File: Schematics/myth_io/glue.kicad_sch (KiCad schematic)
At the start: 4 parts, among them U1 74HC14, U2 74LS02, U5 74AHC04, U6 74HC74

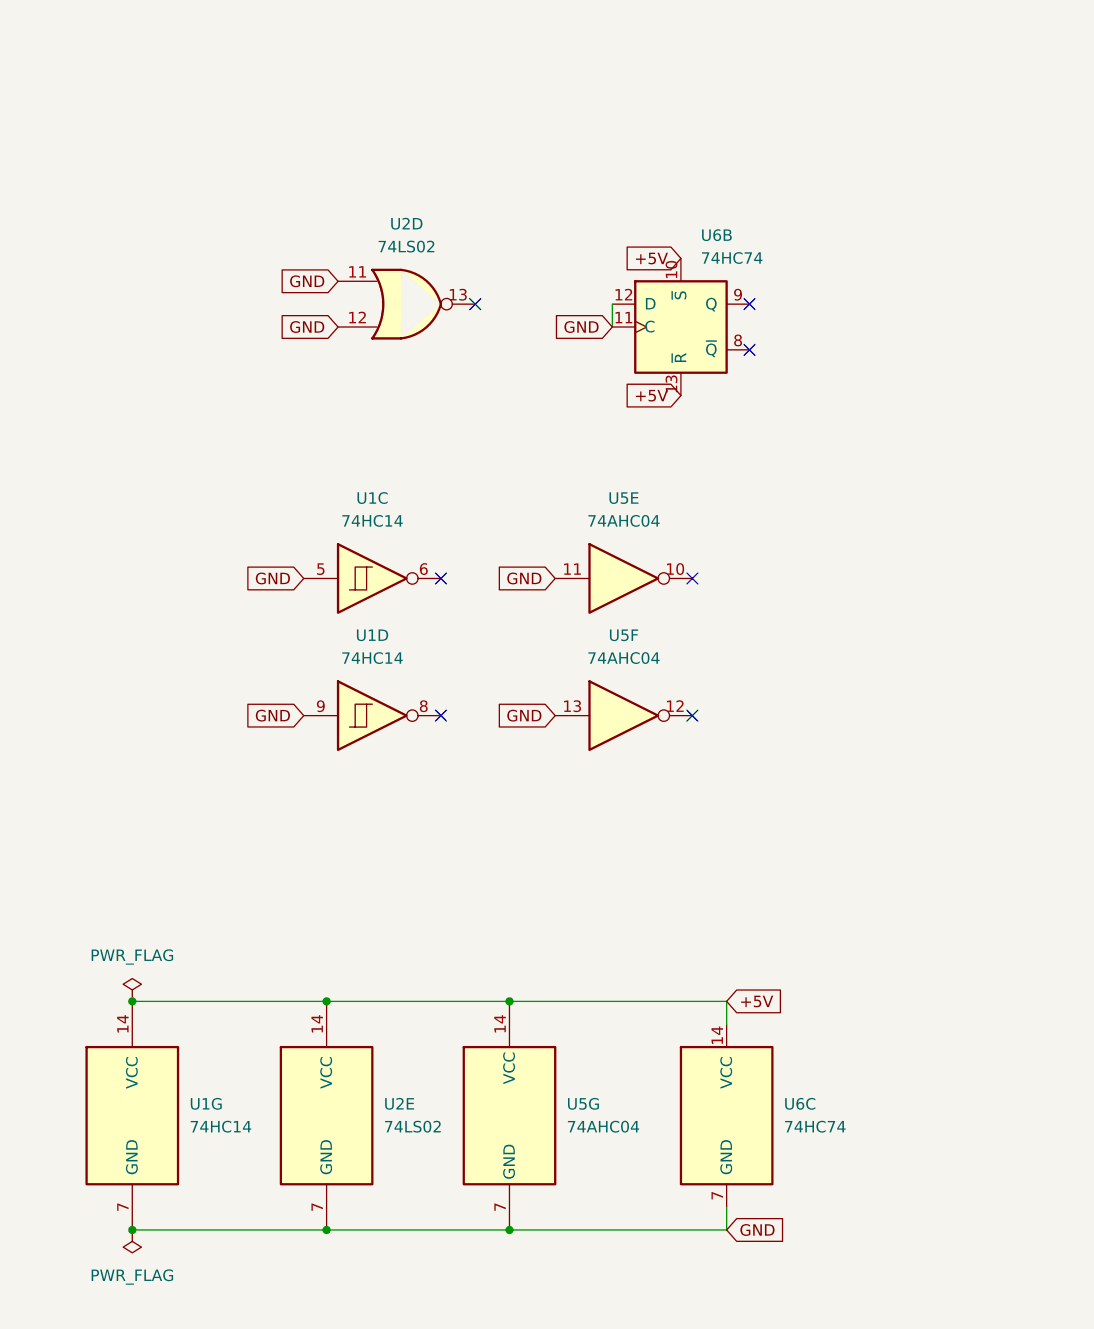
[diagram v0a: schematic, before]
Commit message: Change d to g
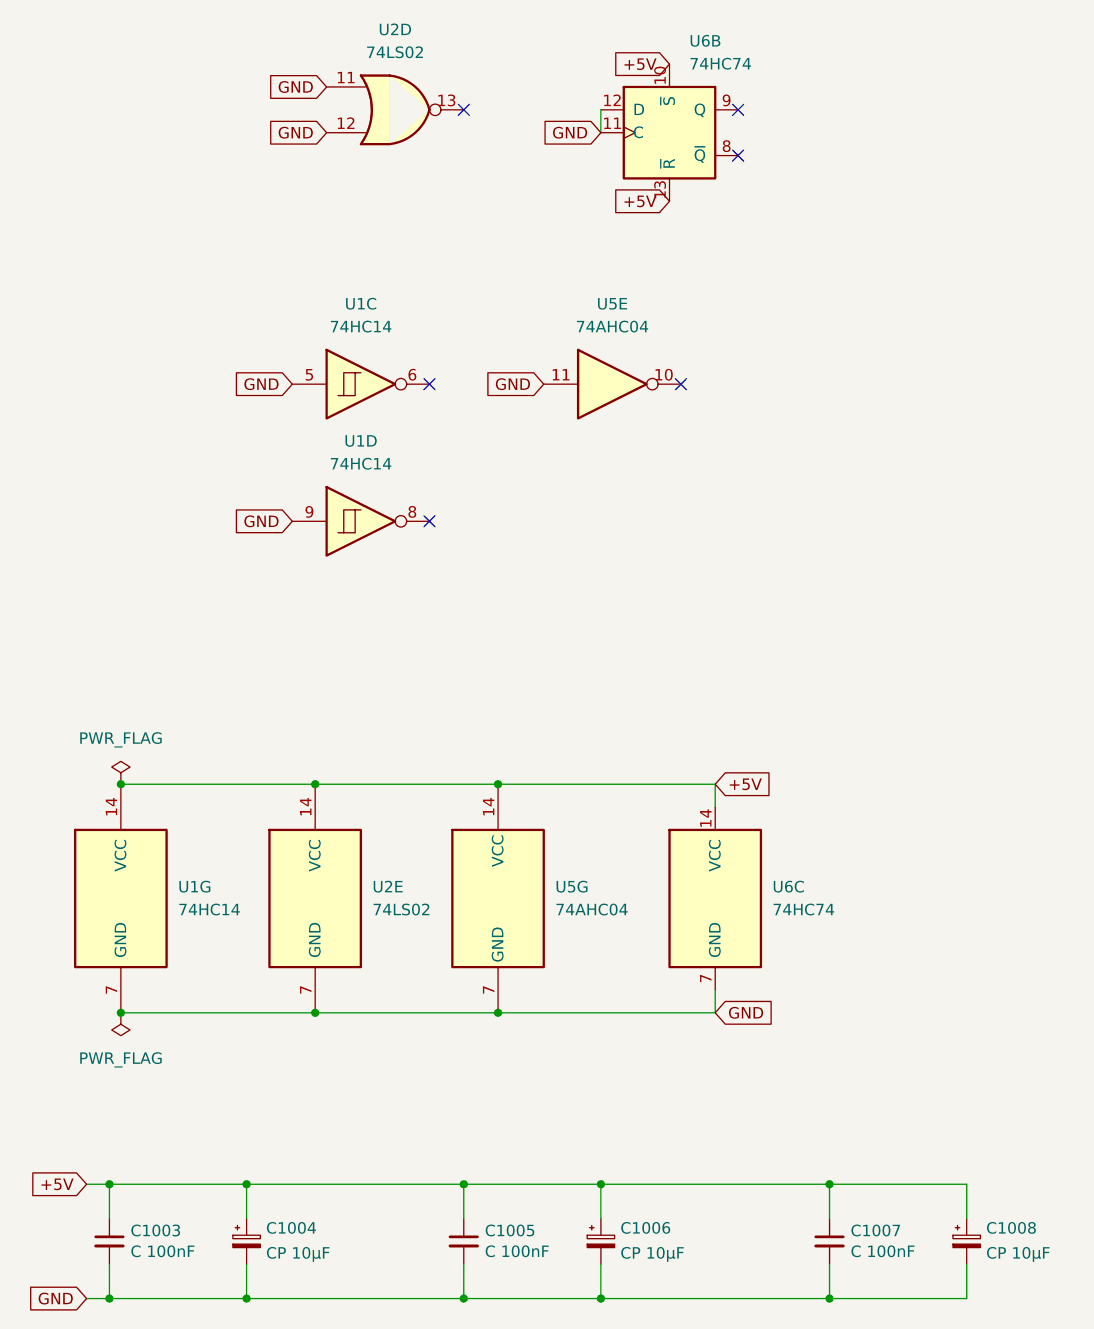
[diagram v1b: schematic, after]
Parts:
- removed unit 6 of U5
- added C1003, C1005, C1007: C 100nF, Capacitor_THT:C_Disc_D5.0mm_W2.5mm_P2.50mm, symbol Device:C_Small
- added C1004, C1006, C1008: CP 10μF, Capacitor_THT:CP_Radial_D6.3mm_P2.50mm, symbol Device:C_Polarized_Small
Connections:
- net +5V: now also C1003.1, C1004.1, C1005.1, C1006.1, C1007.1, C1008.1
- net GND: now also C1003.2, C1004.2, C1005.2, C1006.2, C1007.2, C1008.2
- no-connect marks 7 -> 6
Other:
- moved on the sheet: U1C, U1D, U1G, U2D, U2E, U5E, U5G, U6B, U6C

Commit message: Change CO do D
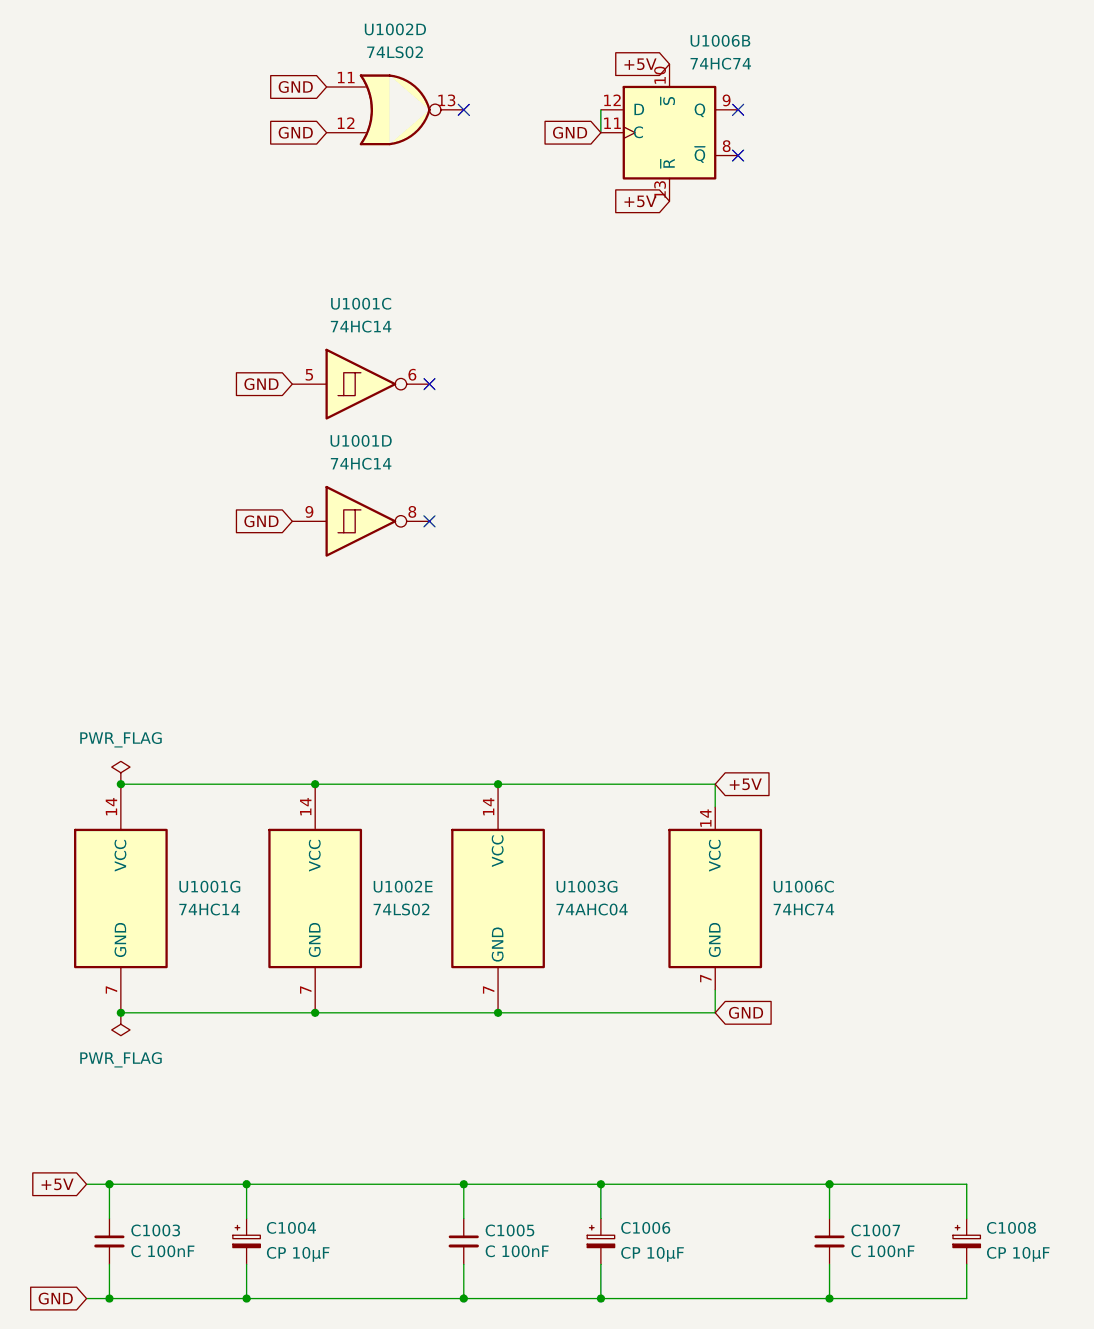
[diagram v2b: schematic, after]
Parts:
- removed unit 5 of U5
- renumbered U1 to U1001, U2 to U1002, U5 to U1003, U6 to U1006
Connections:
- no-connect marks 6 -> 5
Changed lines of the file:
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@@
-	)
-	(no_connect
-		(at 111.76 74.93)
 	)
 	(no_connect
@@
 	(global_label "GND"
 		(shape input)
-		(at 96.52 74.93 180)
+		(at 115.57 144.78 0)
 		(fields_autoplaced yes)
 		(effects
@@
 				(size 1.27 1.27)
 			)
-			(justify right)
+			(justify left)
 		)
 		(property "Intersheetrefs" "${INTERSHEET_REFS}"
-			(at 89.6643 74.93 0)
-			(effects
-				(font
-					(size 1.27 1.27)
-				)
-				(justify right)
+			(at 122.4257 144.78 0)
+			(effects
+				(font
+					(size 1.27 1.27)
+				)
+				(justify left)
 				(hide yes)
 			)
@@
 	(global_label "GND"
 		(shape input)
-		(at 115.57 144.78 0)
+		(at 68.58 90.17 180)
 		(fields_autoplaced yes)
 		(effects
@@
 				(size 1.27 1.27)
 			)
-			(justify left)
-		)
-		(property "Intersheetrefs" "${INTERSHEET_REFS}"
-			(at 122.4257 144.78 0)
-			(effects
-				(font
-					(size 1.27 1.27)
-				)
-				(justify left)
-				(hide yes)
-			)
-		)
-	)
-	(global_label "GND"
-		(shape input)
-		(at 68.58 90.17 180)
-		(fields_autoplaced yes)
-		(effects
-			(font
-				(size 1.27 1.27)
-			)
 			(justify right)
 		)
@@
 				(justify right)
 				(hide yes)
-			)
-		)
-	)
-	(symbol
-		(lib_id "74xx:74AHC04")
-		(at 104.14 74.93 0)
-		(unit 5)
-		(exclude_from_sim no)
-		(in_bom yes)
-		(on_board yes)
-		(dnp no)
-		(fields_autoplaced yes)
-		(property "Reference" "U5"
-			(at 104.14 66.04 0)
-			(effects
-				(font
-					(size 1.27 1.27)
-				)
-			)
-		)
-		(property "Value" "74AHC04"
-			(at 104.14 68.58 0)
-			(effects
-				(font
-					(size 1.27 1.27)
-				)
-			)
-		)
-		(property "Footprint" "Package_DIP:DIP-14_W7.62mm_Socket_LongPads"
-			(at 104.14 74.93 0)
-			(effects
-				(font
-					(size 1.27 1.27)
-				)
-				(hide yes)
-			)
-		)
-		(property "Datasheet" "https://assets.nexperia.com/documents/data-sheet/74AHC_AHCT04.pdf"
-			(at 104.14 74.93 0)
-			(effects
-				(font
-					(size 1.27 1.27)
-				)
-				(hide yes)
-			)
-		)
-		(property "Description" "Hex Inverter"
-			(at 104.14 74.93 0)
-			(effects
-				(font
-					(size 1.27 1.27)
-				)
-				(hide yes)
-			)
-		)
-		(pin "6"
-		)
-		(pin "13"
-		)
-		(pin "14"
-		)
-		(pin "7"
-		)
-		(pin "12"
-		)
-		(pin "1"
-		)
-		(pin "10"
-		)
-		(pin "11"
-		)
-		(pin "5"
-		)
-		(pin "4"
-		)
-		(pin "8"
-		)
-		(pin "2"
-		)
-		(pin "3"
-		)
-		(pin "9"
-		)
-		(instances
-			(project "myth_io"
-				(path "/a907dd88-e0e4-4e6e-a291-053f6213a316/23f7cdcd-5710-47e5-9933-2b44d7b8056b"
-					(reference "U5")
-					(unit 5)
-				)
 			)
 		)
@@
 		(dnp no)
 		(fields_autoplaced yes)
-		(property "Reference" "U2"
+		(property "Reference" "U1002"
 			(at 77.47 130.8099 0)
 			(effects
@@
 			(project "myth_io"
 				(path "/a907dd88-e0e4-4e6e-a291-053f6213a316/23f7cdcd-5710-47e5-9933-2b44d7b8056b"
-					(reference "U2")
+					(reference "U1002")
 					(unit 5)
 				)
@@
 		(dnp no)
 		(fields_autoplaced yes)
-		(property "Reference" "U6"
+		(property "Reference" "U1006"
 			(at 121.92 130.8099 0)
 			(effects
@@
 			(project "myth_io"
 				(path "/a907dd88-e0e4-4e6e-a291-053f6213a316/23f7cdcd-5710-47e5-9933-2b44d7b8056b"
-					(reference "U6")
+					(reference "U1006")
 					(unit 3)
 				)
@@
 		(on_board yes)
 		(dnp no)
-		(property "Reference" "#FLG02"
+		(property "Reference" "#FLG01002"
 			(at 49.53 146.685 0)
 			(effects
@@
 			(project "myth_io"
 				(path "/a907dd88-e0e4-4e6e-a291-053f6213a316/23f7cdcd-5710-47e5-9933-2b44d7b8056b"
-					(reference "#FLG02")
+					(reference "#FLG01002")
 					(unit 1)
 				)
@@
 		(dnp no)
 		(fields_autoplaced yes)
-		(property "Reference" "#FLG01"
+		(property "Reference" "#FLG01001"
 			(at 49.53 117.475 0)
 			(effects
@@
 			(project "myth_io"
 				(path "/a907dd88-e0e4-4e6e-a291-053f6213a316/23f7cdcd-5710-47e5-9933-2b44d7b8056b"
-					(reference "#FLG01")
+					(reference "#FLG01001")
 					(unit 1)
 				)
@@
 		(dnp no)
 		(fields_autoplaced yes)
-		(property "Reference" "U6"
+		(property "Reference" "U1006"
 			(at 112.6841 36.83 0)
 			(effects
@@
 			(project "myth_io"
 				(path "/a907dd88-e0e4-4e6e-a291-053f6213a316/23f7cdcd-5710-47e5-9933-2b44d7b8056b"
-					(reference "U6")
+					(reference "U1006")
 					(unit 2)
 				)
@@
 		(dnp no)
 		(fields_autoplaced yes)
-		(property "Reference" "U5"
+		(property "Reference" "U1003"
 			(at 97.79 130.8099 0)
 			(effects
@@
 			(project "myth_io"
 				(path "/a907dd88-e0e4-4e6e-a291-053f6213a316/23f7cdcd-5710-47e5-9933-2b44d7b8056b"
-					(reference "U5")
+					(reference "U1003")
 					(unit 7)
 				)
@@
 		(dnp no)
 		(fields_autoplaced yes)
-		(property "Reference" "U2"
+		(property "Reference" "U1002"
 			(at 80.01 35.56 0)
 			(effects
@@
 			(project "myth_io"
 				(path "/a907dd88-e0e4-4e6e-a291-053f6213a316/23f7cdcd-5710-47e5-9933-2b44d7b8056b"
-					(reference "U2")
+					(reference "U1002")
 					(unit 4)
 				)
@@
 		(dnp no)
 		(fields_autoplaced yes)
-		(property "Reference" "U1"
+		(property "Reference" "U1001"
 			(at 76.2 81.28 0)
 			(effects
@@
 			(project "myth_io"
 				(path "/a907dd88-e0e4-4e6e-a291-053f6213a316/23f7cdcd-5710-47e5-9933-2b44d7b8056b"
-					(reference "U1")
+					(reference "U1001")
 					(unit 4)
 				)
@@
 		(dnp no)
 		(fields_autoplaced yes)
-		(property "Reference" "U1"
+		(property "Reference" "U1001"
 			(at 55.88 130.8099 0)
 			(effects
@@
 			(project "myth_io"
 				(path "/a907dd88-e0e4-4e6e-a291-053f6213a316/23f7cdcd-5710-47e5-9933-2b44d7b8056b"
-					(reference "U1")
+					(reference "U1001")
 					(unit 7)
 				)
@@
 		(dnp no)
 		(fields_autoplaced yes)
-		(property "Reference" "U1"
+		(property "Reference" "U1001"
 			(at 76.2 66.04 0)
 			(effects
@@
 			(project "myth_io"
 				(path "/a907dd88-e0e4-4e6e-a291-053f6213a316/23f7cdcd-5710-47e5-9933-2b44d7b8056b"
-					(reference "U1")
+					(reference "U1001")
 					(unit 3)
 				)

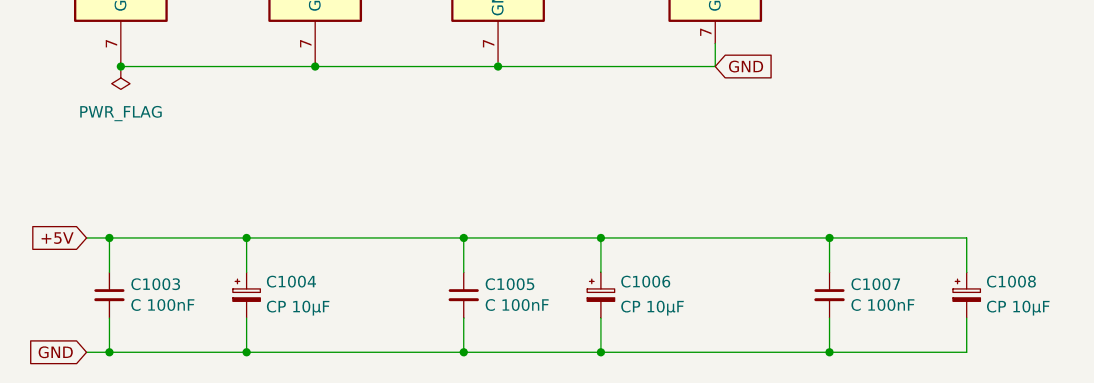
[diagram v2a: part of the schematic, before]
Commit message: Fix documentation re: change d->g
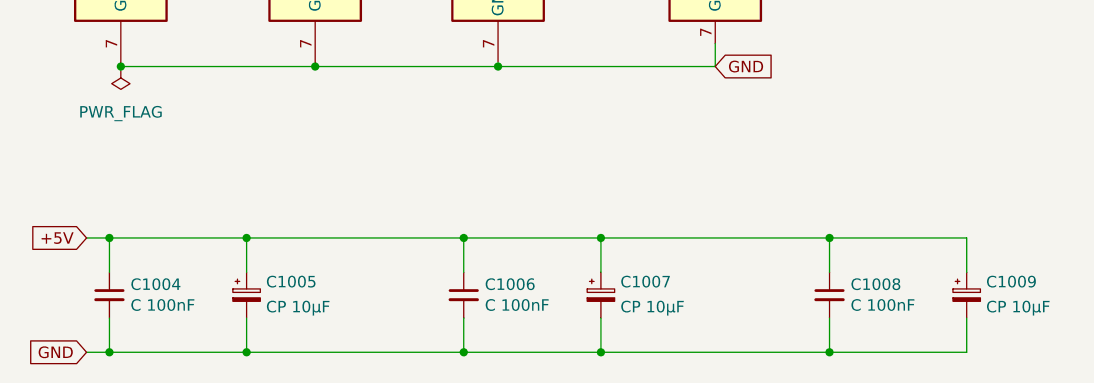
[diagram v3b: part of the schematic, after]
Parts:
- renumbered C1003 to C1004, C1004 to C1005, C1005 to C1006, C1006 to C1007, C1007 to C1008, C1008 to C1009
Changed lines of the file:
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@@
 		(dnp no)
 		(fields_autoplaced yes)
-		(property "Reference" "C1006"
+		(property "Reference" "C1007"
 			(at 105.029 168.7254 0)
 			(effects
@@
 			(project "myth_io"
 				(path "/a907dd88-e0e4-4e6e-a291-053f6213a316/23f7cdcd-5710-47e5-9933-2b44d7b8056b"
-					(reference "C1006")
+					(reference "C1007")
 					(unit 1)
 				)
@@
 		(dnp no)
 		(fields_autoplaced yes)
-		(property "Reference" "C1004"
+		(property "Reference" "C1005"
 			(at 65.659 168.7254 0)
 			(effects
@@
 			(project "myth_io"
 				(path "/a907dd88-e0e4-4e6e-a291-053f6213a316/23f7cdcd-5710-47e5-9933-2b44d7b8056b"
-					(reference "C1004")
+					(reference "C1005")
 					(unit 1)
 				)
@@
 		(dnp no)
 		(fields_autoplaced yes)
-		(property "Reference" "C1008"
+		(property "Reference" "C1009"
 			(at 145.669 168.7254 0)
 			(effects
@@
 			(project "myth_io"
 				(path "/a907dd88-e0e4-4e6e-a291-053f6213a316/23f7cdcd-5710-47e5-9933-2b44d7b8056b"
-					(reference "C1008")
+					(reference "C1009")
 					(unit 1)
 				)
@@
 		(on_board yes)
 		(dnp no)
-		(property "Reference" "C1005"
+		(property "Reference" "C1006"
 			(at 89.9668 169.0116 0)
 			(effects
@@
 			(project "myth_io"
 				(path "/a907dd88-e0e4-4e6e-a291-053f6213a316/23f7cdcd-5710-47e5-9933-2b44d7b8056b"
-					(reference "C1005")
+					(reference "C1006")
 					(unit 1)
 				)
@@
 		(on_board yes)
 		(dnp no)
-		(property "Reference" "C1003"
+		(property "Reference" "C1004"
 			(at 50.5968 169.0116 0)
 			(effects
@@
 			(project "myth_io"
 				(path "/a907dd88-e0e4-4e6e-a291-053f6213a316/23f7cdcd-5710-47e5-9933-2b44d7b8056b"
-					(reference "C1003")
+					(reference "C1004")
 					(unit 1)
 				)
@@
 		(on_board yes)
 		(dnp no)
-		(property "Reference" "C1007"
+		(property "Reference" "C1008"
 			(at 130.6068 169.0116 0)
 			(effects
@@
 			(project "myth_io"
 				(path "/a907dd88-e0e4-4e6e-a291-053f6213a316/23f7cdcd-5710-47e5-9933-2b44d7b8056b"
-					(reference "C1007")
+					(reference "C1008")
 					(unit 1)
 				)
